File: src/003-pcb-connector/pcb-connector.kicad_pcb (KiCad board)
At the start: 2 copper layers, 9 x 19 mm, 7 parts, among them J1 Conn_01x02, J2 Conn_01x02

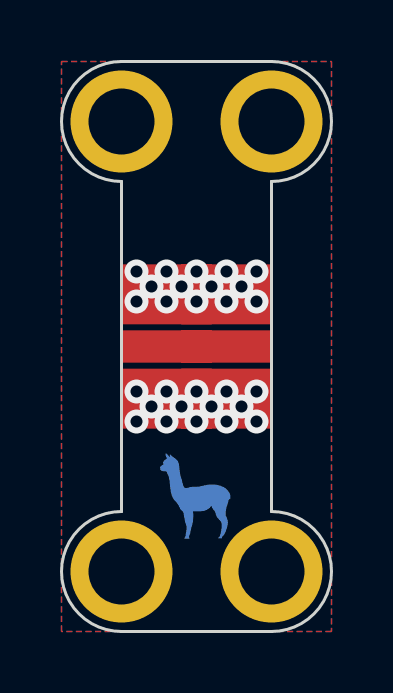
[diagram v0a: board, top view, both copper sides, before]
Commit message: changing pcb connector
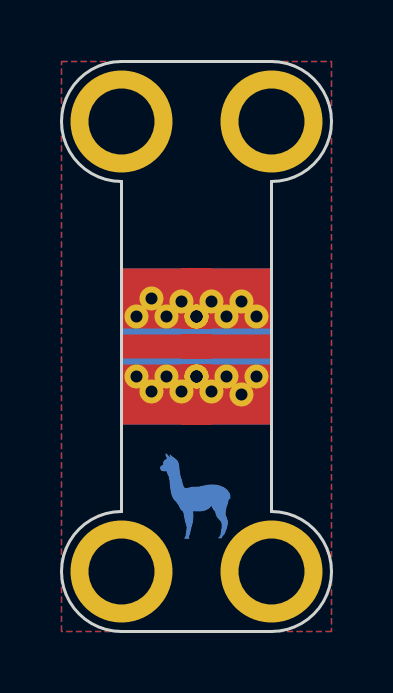
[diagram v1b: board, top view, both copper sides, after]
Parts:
- J1, J2: value Conn_01x02 -> CONN
- moved J1 5.00 mm to (145.0, 82.5), turned to 180 degrees
- moved J2 5.00 mm to (150.0, 82.5), turned to 0 degrees
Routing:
- net GND: vias 28 -> 0
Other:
- outline, holes or cut-outs redrawn
- board text added: "003"
